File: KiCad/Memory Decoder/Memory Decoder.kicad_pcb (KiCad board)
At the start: 2 copper layers, 55.1 x 36.1 mm, 11 parts, among them J1 IOCS/Decoder Signals Expansio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, J2 Conn_02x02_Odd_Even, J3 Decoder Signals, J4 Conn_02x03_Odd_Even, J5 Memory Decoder Expansion, J6 ~CS1~, J7 ~CS1~, SW1 SW_DIP_x04, SW2 SW_DIP_x04, U1 Flexible Memory Decoder

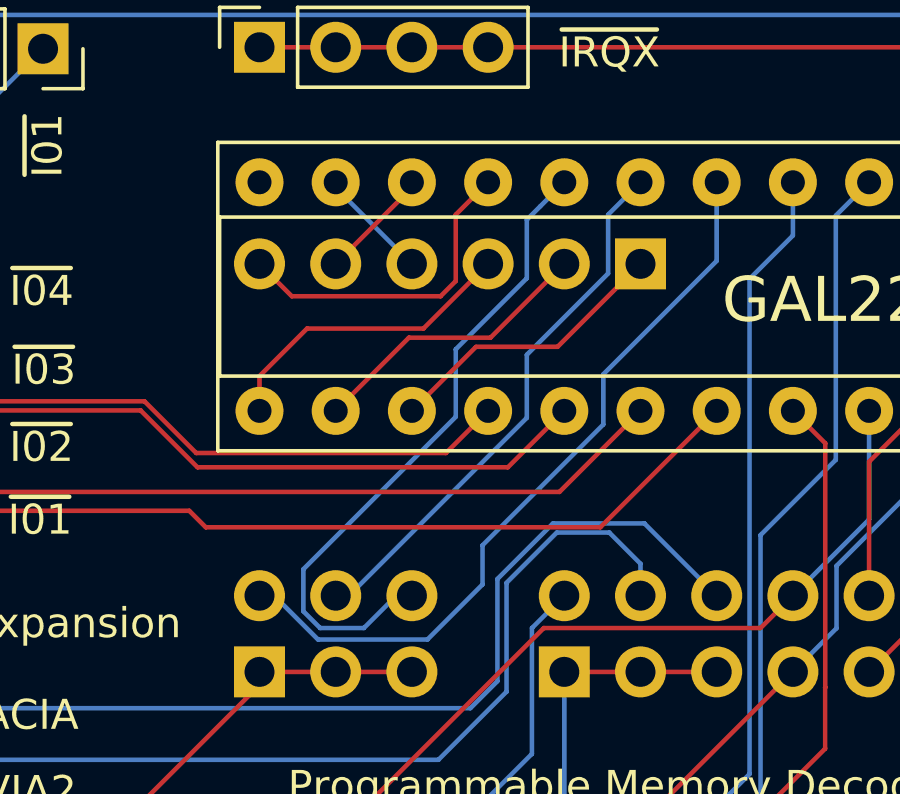
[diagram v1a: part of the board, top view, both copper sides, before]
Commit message: memory decoder revised
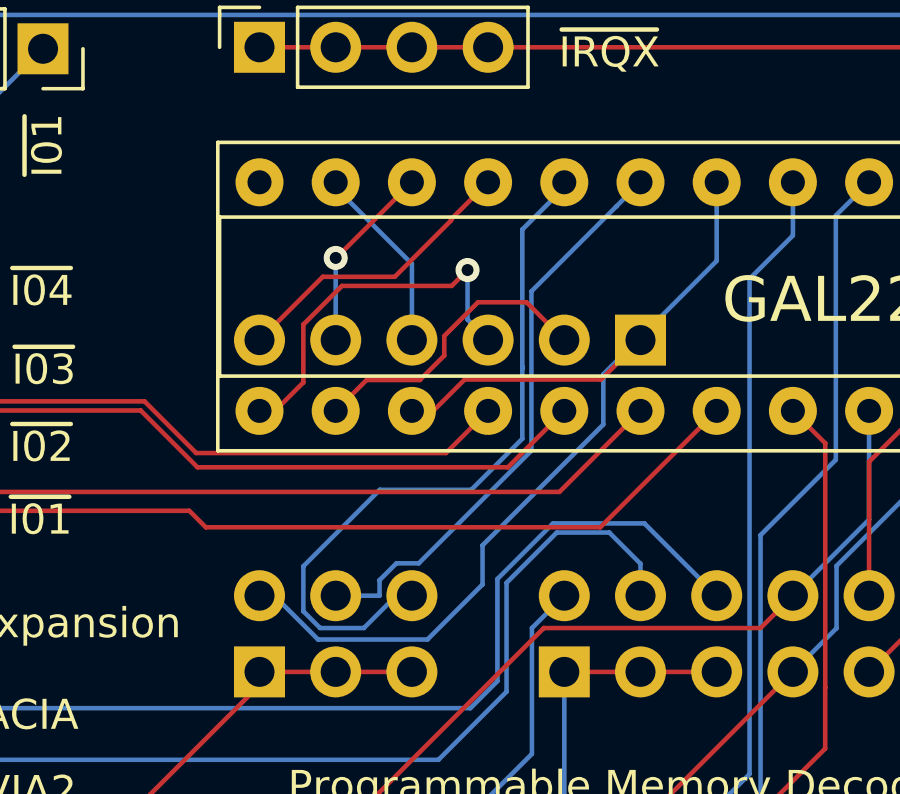
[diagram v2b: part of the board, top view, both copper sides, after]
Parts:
- moved J5 2.54 mm to (133.3, 86.5)
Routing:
- net /a8: track 3.77 -> 6.32 mm, vias 0 -> 1
- net /a7: track 3.77 -> 6.31 mm
- net /a6: track 10.3 -> 12.6 mm, vias 0 -> 1
- net /a10: track 22.2 -> 24.1 mm
- net /a9: track 10.9 -> 9.82 mm
- net /a4: track 9.65 -> 8.60 mm
- net /a11: track 18.2 -> 19.3 mm

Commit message: Rev004 revisions
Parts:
- moved J1 2.54 mm to (128.2, 97.6)
- moved J5 0.53 mm to (133.3, 86.0)
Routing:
- net ~IOCS_V2: track 32.9 -> 27.4 mm, vias 0 -> 1
- net RAM~WE: track 9.75 -> 12.3 mm
- net ~ROM_CS: track 25.0 -> 22.8 mm
- net ~RAM_OE: track 35.8 -> 37.5 mm
- net /a12: track 25.4 -> 27.2 mm
- net /a14: track 26.0 -> 27.3 mm
- net R~W: track 15.9 -> 16.9 mm
- net ~RAM_CS: track 27.9 -> 28.9 mm
- net ~IOCS_A: track 33.9 -> 33.0 mm
- net /a5: track 10.0 -> 10.6 mm
- net ~RES: track 69.4 -> 70.0 mm
- net /a8: track 6.32 -> 5.79 mm
- net /a7: track 6.31 -> 5.78 mm
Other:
- board text added: "C1"

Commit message: Rev004 updates
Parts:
- added REF**: OSHW-Logo2_7.3x6mm_SilkScreen, Symbol:OSHW-Logo2_7.3x6mm_SilkScreen, B.Cu at (113.7, 82.9)
- added REF**: KiCad-Logo2_5mm_SilkScreen, Symbol:KiCad-Logo2_5mm_SilkScreen, B.Cu at (113.5, 101.3)
